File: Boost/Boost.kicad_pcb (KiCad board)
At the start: 2 copper layers, 93 parts, among them P1 CONN_01X02, P2 TST, P3 TST, P4 CONN_01X02, U1 TSP61087

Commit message: Created Gerbers and stinsil file
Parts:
- removed REF**121111, REF**1211110, REF**121112, REF**121113, REF**121114, REF**121115, REF**121116, REF**121117, REF**121118, REF**121119, REF**121121, REF**1211210, REF**121122, REF**121123, REF**121124, REF**121125, REF**121126, REF**121127, REF**121128, REF**121129, REF**1211310, REF**121132, REF**121133, REF**121134, REF**121135, REF**121136, REF**121137, REF**121138, REF**121139, REF**121141, REF**1211410, REF**1211411, REF**1211412, REF**121143, REF**121144, REF**121145, REF**121146, REF**121147, REF**121148, REF**121149, REF**121151, REF**1211510, REF**1211511, REF**1211512, REF**121152, REF**121154, REF**121155, REF**121156, REF**121157, REF**121158, REF**121159, REF**121161, REF**1211612, REF**121162, REF**121163, REF**121165, REF**121171, REF**121172, REF**121173, REF**121175, REF**1212, REF**1213, REF**1221, REF**1222, REF**1223, REF**1225, REF**1231, REF**1232, REF**1233, REF**1235, REF**1243: VIA-0.6mm, Boost-Footprints:VIA-0.6mm
- added G***: LOGO, Boost-Footprints:KiCadLogo-17x6, B.Cu at (147.9, 94.1)
- added REF**121111112: VIA-0.6mm, Boost-Footprints:VIA-0.6mm, F.Cu at (151.2, 88.1)
- added REF**121111113: VIA-0.6mm, Boost-Footprints:VIA-0.6mm, F.Cu at (151.2, 90.1)
- added REF**121111121: VIA-0.6mm, Boost-Footprints:VIA-0.6mm, F.Cu at (153.2, 86.1)
- added REF**121111122: VIA-0.6mm, Boost-Footprints:VIA-0.6mm, F.Cu at (153.2, 88.1)
- added REF**121111123: VIA-0.6mm, Boost-Footprints:VIA-0.6mm, F.Cu at (153.2, 90.1)
- added REF**121111125: VIA-0.6mm, Boost-Footprints:VIA-0.6mm, F.Cu at (153.2, 94.1)
- added REF**121111131: VIA-0.6mm, Boost-Footprints:VIA-0.6mm, F.Cu at (155.2, 86.1)
- added REF**121111132: VIA-0.6mm, Boost-Footprints:VIA-0.6mm, F.Cu at (155.2, 88.1)
- added REF**121111133: VIA-0.6mm, Boost-Footprints:VIA-0.6mm, F.Cu at (155.2, 90.1)
- added REF**121111135: VIA-0.6mm, Boost-Footprints:VIA-0.6mm, F.Cu at (155.2, 94.1)
- added REF**121111143: VIA-0.6mm, Boost-Footprints:VIA-0.6mm, F.Cu at (157.2, 90.1)
- added REF**12111131111: VIA-0.6mm, Boost-Footprints:VIA-0.6mm, F.Cu at (145.7, 106.5)
- added REF**121111311110: VIA-0.6mm, Boost-Footprints:VIA-0.6mm, F.Cu at (145.7, 124.5)
- added REF**12111131112: VIA-0.6mm, Boost-Footprints:VIA-0.6mm, F.Cu at (145.7, 108.5)
- added REF**12111131113: VIA-0.6mm, Boost-Footprints:VIA-0.6mm, F.Cu at (145.7, 110.5)
- added REF**12111131114: VIA-0.6mm, Boost-Footprints:VIA-0.6mm, F.Cu at (145.7, 112.5)
- added REF**12111131115: VIA-0.6mm, Boost-Footprints:VIA-0.6mm, F.Cu at (145.7, 114.5)
- added REF**12111131116: VIA-0.6mm, Boost-Footprints:VIA-0.6mm, F.Cu at (145.7, 116.5)
- added REF**12111131117: VIA-0.6mm, Boost-Footprints:VIA-0.6mm, F.Cu at (145.7, 118.5)
- added REF**12111131118: VIA-0.6mm, Boost-Footprints:VIA-0.6mm, F.Cu at (145.7, 120.5)
- added REF**12111131119: VIA-0.6mm, Boost-Footprints:VIA-0.6mm, F.Cu at (145.7, 122.5)
- added REF**12111131121: VIA-0.6mm, Boost-Footprints:VIA-0.6mm, F.Cu at (147.7, 106.5)
- added REF**121111311210: VIA-0.6mm, Boost-Footprints:VIA-0.6mm, F.Cu at (147.7, 124.5)
- added REF**12111131122: VIA-0.6mm, Boost-Footprints:VIA-0.6mm, F.Cu at (147.7, 108.5)
- added REF**12111131123: VIA-0.6mm, Boost-Footprints:VIA-0.6mm, F.Cu at (147.7, 110.5)
- added REF**12111131124: VIA-0.6mm, Boost-Footprints:VIA-0.6mm, F.Cu at (147.7, 112.5)
- added REF**12111131125: VIA-0.6mm, Boost-Footprints:VIA-0.6mm, F.Cu at (147.7, 114.5)
- added REF**12111131126: VIA-0.6mm, Boost-Footprints:VIA-0.6mm, F.Cu at (147.7, 116.5)
- added REF**12111131127: VIA-0.6mm, Boost-Footprints:VIA-0.6mm, F.Cu at (147.7, 118.5)
- added REF**12111131128: VIA-0.6mm, Boost-Footprints:VIA-0.6mm, F.Cu at (147.7, 120.5)
- added REF**12111131129: VIA-0.6mm, Boost-Footprints:VIA-0.6mm, F.Cu at (147.7, 122.5)
- added REF**121111311310: VIA-0.6mm, Boost-Footprints:VIA-0.6mm, F.Cu at (149.7, 124.5)
- added REF**12111131132: VIA-0.6mm, Boost-Footprints:VIA-0.6mm, F.Cu at (149.7, 108.5)
- added REF**12111131133: VIA-0.6mm, Boost-Footprints:VIA-0.6mm, F.Cu at (149.7, 110.5)
- added REF**12111131134: VIA-0.6mm, Boost-Footprints:VIA-0.6mm, F.Cu at (149.7, 112.5)
- added REF**12111131135: VIA-0.6mm, Boost-Footprints:VIA-0.6mm, F.Cu at (149.7, 114.5)
- added REF**12111131136: VIA-0.6mm, Boost-Footprints:VIA-0.6mm, F.Cu at (149.7, 116.5)
- added REF**12111131137: VIA-0.6mm, Boost-Footprints:VIA-0.6mm, F.Cu at (149.7, 118.5)
- added REF**12111131138: VIA-0.6mm, Boost-Footprints:VIA-0.6mm, F.Cu at (149.7, 120.5)
- added REF**12111131139: VIA-0.6mm, Boost-Footprints:VIA-0.6mm, F.Cu at (149.7, 122.5)
- added REF**12111131141: VIA-0.6mm, Boost-Footprints:VIA-0.6mm, F.Cu at (151.7, 106.5)
- added REF**121111311410: VIA-0.6mm, Boost-Footprints:VIA-0.6mm, F.Cu at (151.7, 124.5)
- added REF**121111311411: VIA-0.6mm, Boost-Footprints:VIA-0.6mm, F.Cu at (151.7, 126.5)
- added REF**121111311412: VIA-0.6mm, Boost-Footprints:VIA-0.6mm, F.Cu at (151.7, 128.5)
- added REF**121111311413: VIA-0.6mm, Boost-Footprints:VIA-0.6mm, F.Cu at (151.7, 130.5)
- added REF**12111131143: VIA-0.6mm, Boost-Footprints:VIA-0.6mm, F.Cu at (151.7, 110.5)
- added REF**12111131144: VIA-0.6mm, Boost-Footprints:VIA-0.6mm, F.Cu at (151.7, 112.5)
- added REF**12111131145: VIA-0.6mm, Boost-Footprints:VIA-0.6mm, F.Cu at (151.7, 114.5)
- added REF**12111131146: VIA-0.6mm, Boost-Footprints:VIA-0.6mm, F.Cu at (151.7, 116.5)
- added REF**12111131147: VIA-0.6mm, Boost-Footprints:VIA-0.6mm, F.Cu at (151.7, 118.5)
- added REF**12111131148: VIA-0.6mm, Boost-Footprints:VIA-0.6mm, F.Cu at (151.7, 120.5)
- added REF**12111131149: VIA-0.6mm, Boost-Footprints:VIA-0.6mm, F.Cu at (151.7, 122.5)
- added REF**12111131151: VIA-0.6mm, Boost-Footprints:VIA-0.6mm, F.Cu at (153.7, 105.0)
- added REF**12111131151: VIA-0.6mm, Boost-Footprints:VIA-0.6mm, F.Cu at (153.7, 106.5)
- added REF**121111311510: VIA-0.6mm, Boost-Footprints:VIA-0.6mm, F.Cu at (153.7, 124.5)
- added REF**121111311511: VIA-0.6mm, Boost-Footprints:VIA-0.6mm, F.Cu at (153.7, 126.5)
- added REF**121111311512: VIA-0.6mm, Boost-Footprints:VIA-0.6mm, F.Cu at (153.7, 128.5)
- added REF**121111311513: VIA-0.6mm, Boost-Footprints:VIA-0.6mm, F.Cu at (153.7, 130.5)
- added REF**12111131152: VIA-0.6mm, Boost-Footprints:VIA-0.6mm, F.Cu at (153.7, 108.5)
- added REF**12111131154: VIA-0.6mm, Boost-Footprints:VIA-0.6mm, F.Cu at (153.7, 112.5)
- added REF**12111131155: VIA-0.6mm, Boost-Footprints:VIA-0.6mm, F.Cu at (153.7, 114.5)
- added REF**12111131156: VIA-0.6mm, Boost-Footprints:VIA-0.6mm, F.Cu at (153.7, 116.5)
- added REF**12111131157: VIA-0.6mm, Boost-Footprints:VIA-0.6mm, F.Cu at (153.7, 118.5)
- added REF**12111131158: VIA-0.6mm, Boost-Footprints:VIA-0.6mm, F.Cu at (153.7, 120.5)
- added REF**12111131159: VIA-0.6mm, Boost-Footprints:VIA-0.6mm, F.Cu at (153.7, 122.5)
- added REF**12111131161: VIA-0.6mm, Boost-Footprints:VIA-0.6mm, F.Cu at (155.7, 105.0)
- added REF**12111131161: VIA-0.6mm, Boost-Footprints:VIA-0.6mm, F.Cu at (155.7, 106.5)
- added REF**121111311611: VIA-0.6mm, Boost-Footprints:VIA-0.6mm, F.Cu at (155.7, 126.5)
- added REF**121111311612: VIA-0.6mm, Boost-Footprints:VIA-0.6mm, F.Cu at (155.7, 128.5)
- added REF**121111311613: VIA-0.6mm, Boost-Footprints:VIA-0.6mm, F.Cu at (155.7, 130.5)
- added REF**12111131162: VIA-0.6mm, Boost-Footprints:VIA-0.6mm, F.Cu at (155.7, 108.5)
- added REF**12111131163: VIA-0.6mm, Boost-Footprints:VIA-0.6mm, F.Cu at (155.7, 110.5)
- added REF**12111131165: VIA-0.6mm, Boost-Footprints:VIA-0.6mm, F.Cu at (155.7, 114.5)
- added REF**12111131171: VIA-0.6mm, Boost-Footprints:VIA-0.6mm, F.Cu at (157.7, 106.5)
- added REF**12111131172: VIA-0.6mm, Boost-Footprints:VIA-0.6mm, F.Cu at (157.7, 108.5)
- added REF**12111131173: VIA-0.6mm, Boost-Footprints:VIA-0.6mm, F.Cu at (157.7, 110.5)
- added REF**12111131175: VIA-0.6mm, Boost-Footprints:VIA-0.6mm, F.Cu at (157.7, 114.5)
- moved P3 2.29 mm to (166.0, 128.9)
- moved P2 1.32 mm to (165.8, 87.4)
- moved REF**121111111 0.41 mm to (151.2, 86.1)
- renumbered REF**1211 to REF**121111111
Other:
- board outline added: 33.2 x 46.3 mm

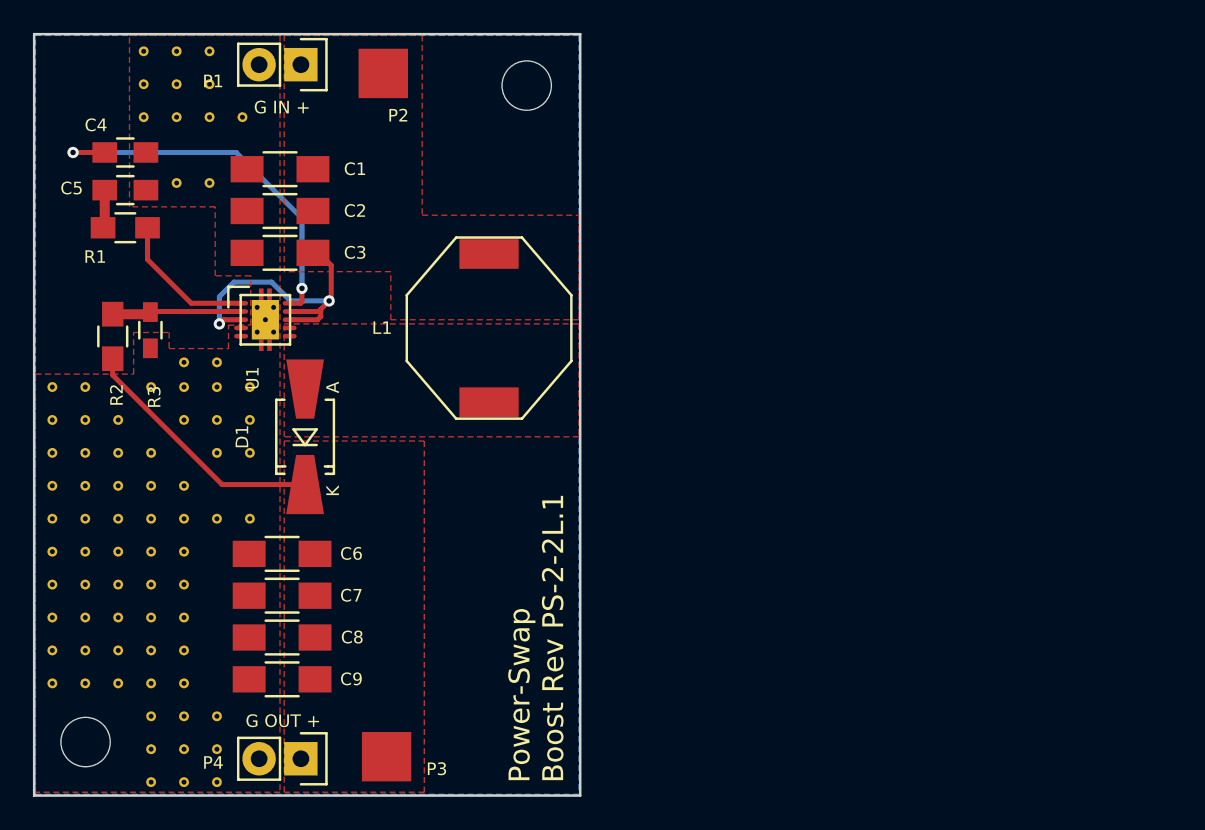
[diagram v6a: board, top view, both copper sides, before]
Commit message: Cleaned up the layout in preperation for gerbers. Made some pads solid rather than from parent
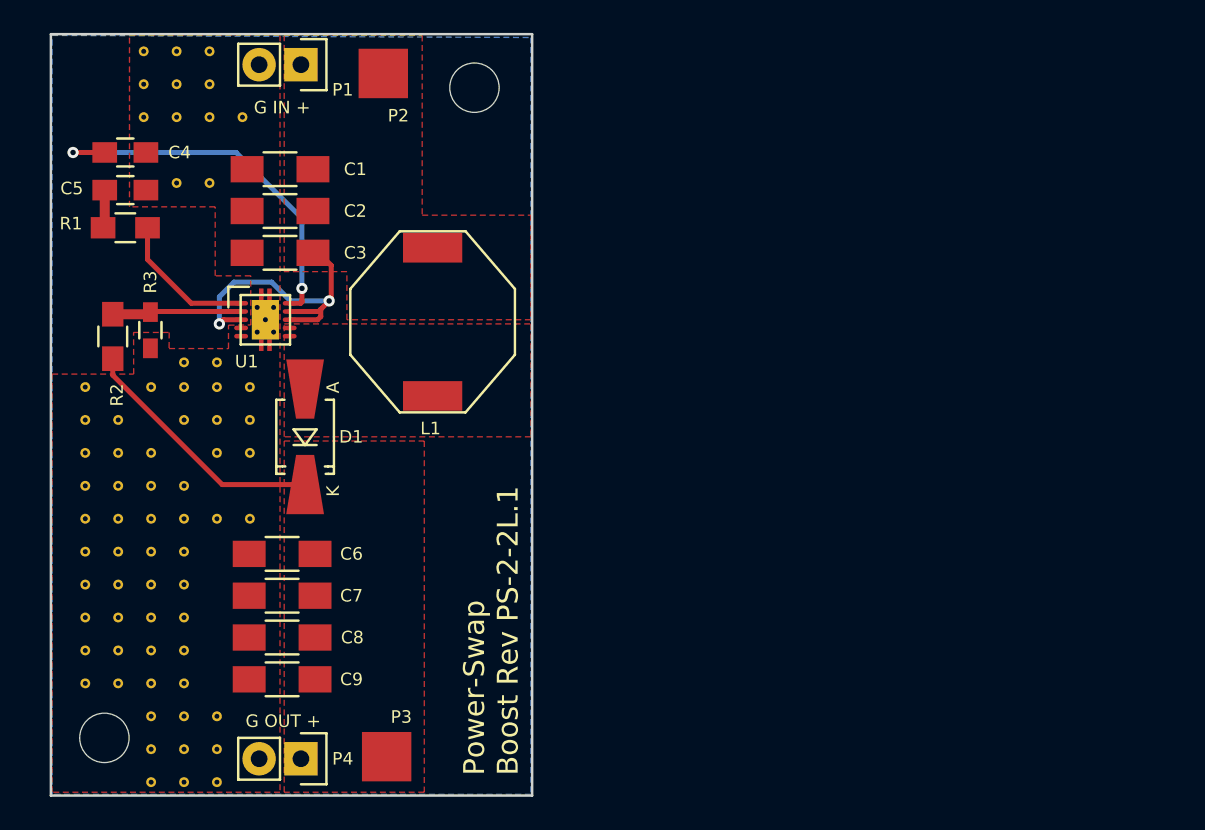
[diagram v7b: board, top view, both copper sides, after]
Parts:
- removed REF**12111131111, REF**121111311110, REF**12111131112, REF**12111131113, REF**12111131114, REF**12111131115, REF**12111131116, REF**12111131117, REF**12111131118, REF**12111131119: VIA-0.6mm, Boost-Footprints:VIA-0.6mm
- moved L1 3.45 mm to (168.8, 102.5)
- moved REF** 3.18 mm to (171.3, 88.3)
- moved REF** 1.17 mm to (148.8, 127.8)
- moved G*** 0.95 mm to (148.8, 94.2)
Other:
- board size 33.2 x 46.3 mm -> 29.2 x 46.3 mm
